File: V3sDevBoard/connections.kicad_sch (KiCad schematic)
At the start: 12 parts, among them J1 JST_ETHERNET, J2 USB_C_Receptacle_USB2.0_16P, J3 USB_C_Receptacle_USB2.0_16P, U5 CH340C

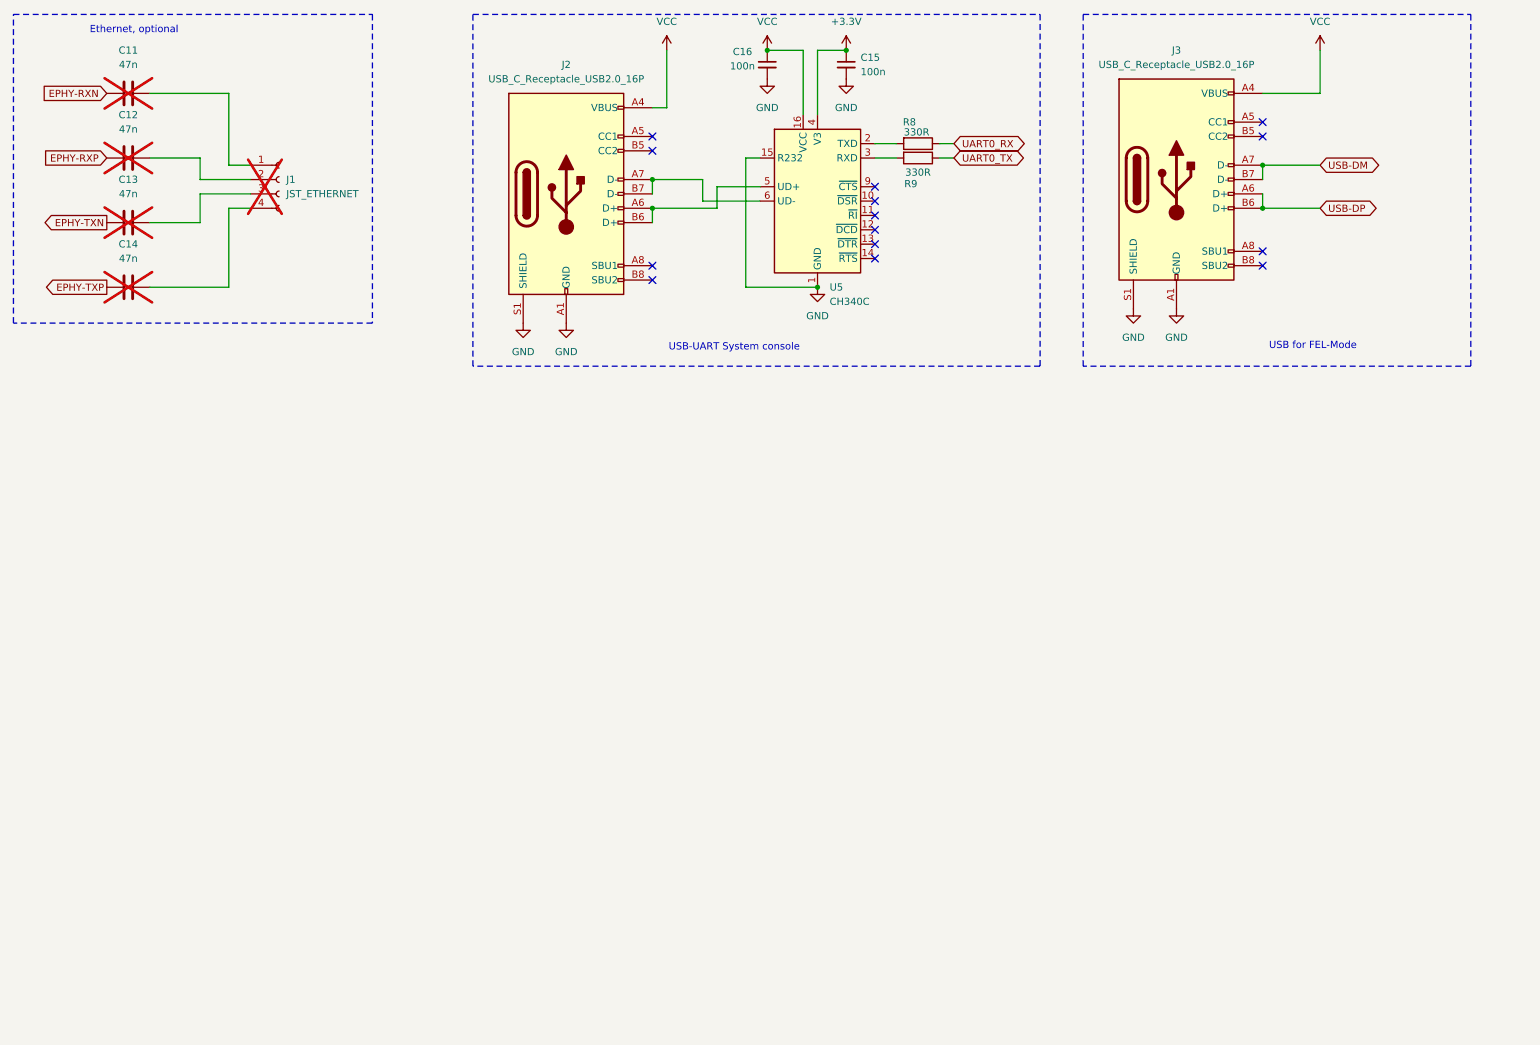
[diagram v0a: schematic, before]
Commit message: drawing schematic
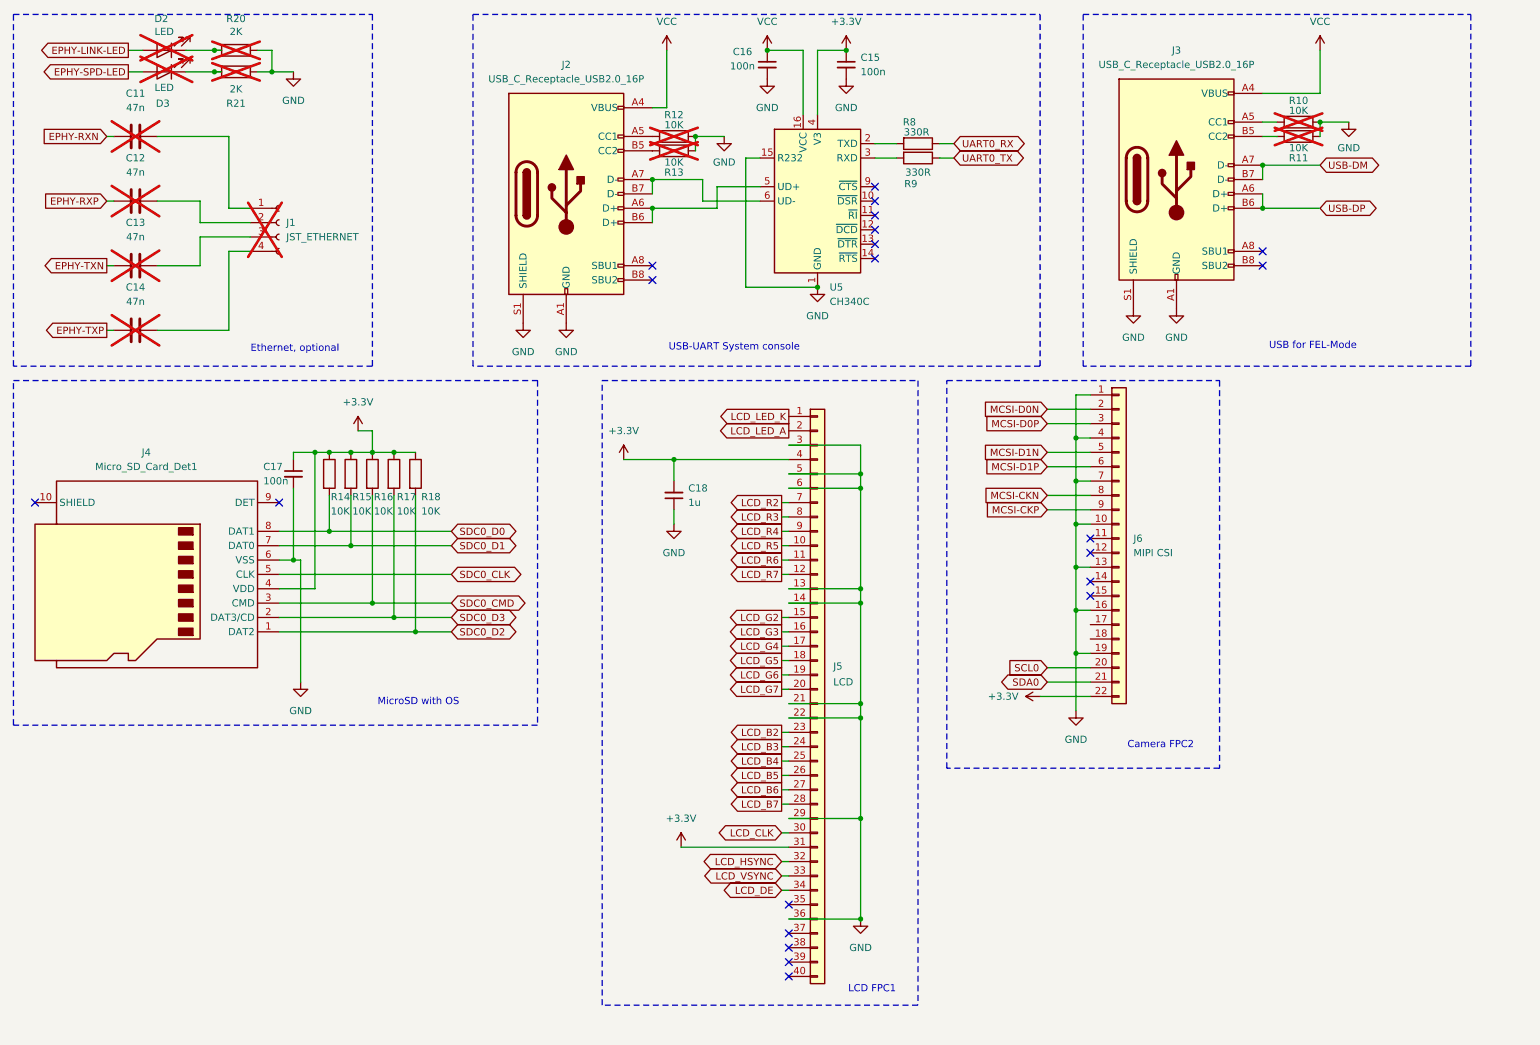
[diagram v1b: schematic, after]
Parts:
- added C17: 100n, symbol Device:C_Small
- added C18: 1u, symbol Device:C_Small
- added D2, D3: LED, LED_SMD:LED_0805_2012Metric_Pad1.15x1.40mm_HandSolder, symbol Device:LED
- added J4: Micro_SD_Card_Det1, symbol Connector:Micro_SD_Card_Det1
- added J5: LCD, Connector_FFC-FPC:Amphenol_F32Q-1A7x1-11040_1x40-1MP_P0.5mm_Horizontal, symbol Connector_Generic:Conn_01x40
- added J6: MIPI CSI, symbol Connector_Generic:Conn_01x22
- added R10, R11, R12, R13, R14, R15, R16, R17, R18: 10K, Resistor_SMD:R_0805_2012Metric_Pad1.20x1.40mm_HandSolder, symbol Device:R
- added R20, R21: 2K, Resistor_SMD:R_0805_2012Metric_Pad1.20x1.40mm_HandSolder, symbol Device:R
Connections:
- net +3.3V: now also C17.1, C18.2, J4.4 (VDD), J5.31 (Pin_31), J5.4 (Pin_4), J6.22 (Pin_22), R14.1, R15.1, R16.1, R17.1, R18.1
- net GND: now also C17.2, C18.1, J4.6 (VSS), J5.13 (Pin_13), J5.14 (Pin_14), J5.21 (Pin_21), J5.22 (Pin_22), J5.29 (Pin_29), J5.3 (Pin_3), J5.36 (Pin_36), J5.5 (Pin_5), J5.6 (Pin_6), J6.1 (Pin_1), J6.10 (Pin_10), J6.13 (Pin_13), J6.16 (Pin_16), J6.19 (Pin_19), J6.4 (Pin_4), J6.7 (Pin_7), R10.2, R11.1, R12.2, R13.1, R20.2, R21.1
- net at J2.A5 (CC1): now also R12.1
- net at J2.B5 (CC2): now also R13.2
- net at J3.A5 (CC1): now also R10.1
- net at J3.B5 (CC2): now also R11.2
- new net: D2.1 (K), R20.1
- new net: D3.1 (K), R21.2
- new net EPHY-LINK-LED: D2.2 (A)
- new net EPHY-SPD-LED: D3.2 (A)
- new net LCD_B2: J5.23 (Pin_23)
- new net LCD_B3: J5.24 (Pin_24)
- new net LCD_B4: J5.25 (Pin_25)
- new net LCD_B5: J5.26 (Pin_26)
- new net LCD_B6: J5.27 (Pin_27)
- new net LCD_B7: J5.28 (Pin_28)
- new net LCD_CLK: J5.30 (Pin_30)
- new net LCD_DE: J5.34 (Pin_34)
- new net LCD_G2: J5.15 (Pin_15)
- new net LCD_G3: J5.16 (Pin_16)
- new net LCD_G4: J5.17 (Pin_17)
- new net LCD_G5: J5.18 (Pin_18)
- new net LCD_G6: J5.19 (Pin_19)
- new net LCD_G7: J5.20 (Pin_20)
- new net LCD_HSYNC: J5.32 (Pin_32)
- new net LCD_LED_A: J5.2 (Pin_2)
- new net LCD_LED_K: J5.1 (Pin_1)
- new net LCD_R2: J5.7 (Pin_7)
- new net LCD_R3: J5.8 (Pin_8)
- new net LCD_R4: J5.9 (Pin_9)
- new net LCD_R5: J5.10 (Pin_10)
- new net LCD_R6: J5.11 (Pin_11)
- new net LCD_R7: J5.12 (Pin_12)
- new net LCD_VSYNC: J5.33 (Pin_33)
- new net MCSI-CKN: J6.8 (Pin_8)
- new net MCSI-CKP: J6.9 (Pin_9)
- new net MCSI-D0N: J6.2 (Pin_2)
- new net MCSI-D0P: J6.3 (Pin_3)
- new net MCSI-D1N: J6.5 (Pin_5)
- new net MCSI-D1P: J6.6 (Pin_6)
- new net SCL0: J6.20 (Pin_20)
- new net SDA0: J6.21 (Pin_21)
- new net SDC0_CLK: J4.5 (CLK)
- new net SDC0_CMD: J4.3 (CMD), R16.2
- new net SDC0_D0: J4.8 (DAT1), R14.2
- new net SDC0_D1: J4.7 (DAT0), R15.2
- new net SDC0_D2: J4.1 (DAT2), R18.2
- new net SDC0_D3: J4.2 (DAT3/CD), R17.2
- no-connect marks 14 -> 21
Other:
- note added: "Camera FPC2"
- note added: "LCD FPC1"
- note added: "MicroSD with OS"
- moved on the sheet: C11, C12, C13, C14, J1

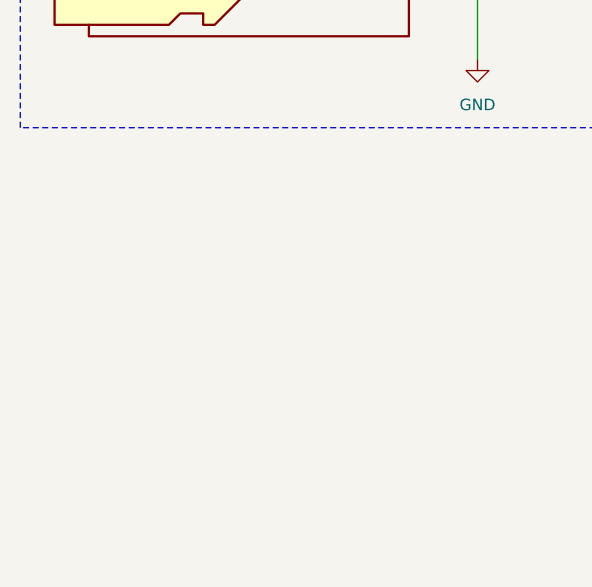
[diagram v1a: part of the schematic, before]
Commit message: drawing schematics
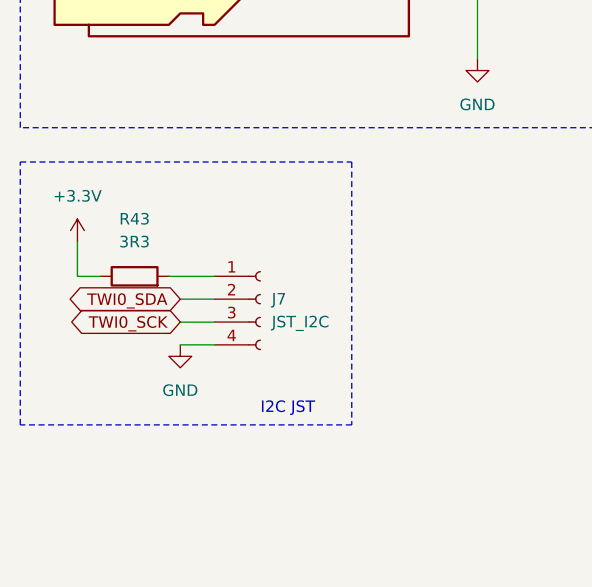
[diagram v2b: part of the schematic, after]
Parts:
- added J7: JST_I2C, Connector_JST:JST_GH_BM04B-GHS-TBT_1x04-1MP_P1.25mm_Vertical, symbol Connector:Conn_01x04_Socket
- added R43: 3R3, symbol Device:R
- J6: footprint (none) -> Connector_FFC-FPC:Amphenol_F32Q-1A7x1-11022_1x22-1MP_P0.5mm_Horizontal
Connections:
- net +3.3V: now also R43.1
- net GND: now also J7.4 (Pin_4)
- new net: J7.1 (Pin_1), R43.2
- new net TWI0_SCK: J7.3 (Pin_3)
- new net TWI0_SDA: J7.2 (Pin_2)
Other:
- note added: "I2C JST"
- company: (none) -> J.K.
- title: (none) -> V3s Dev Board

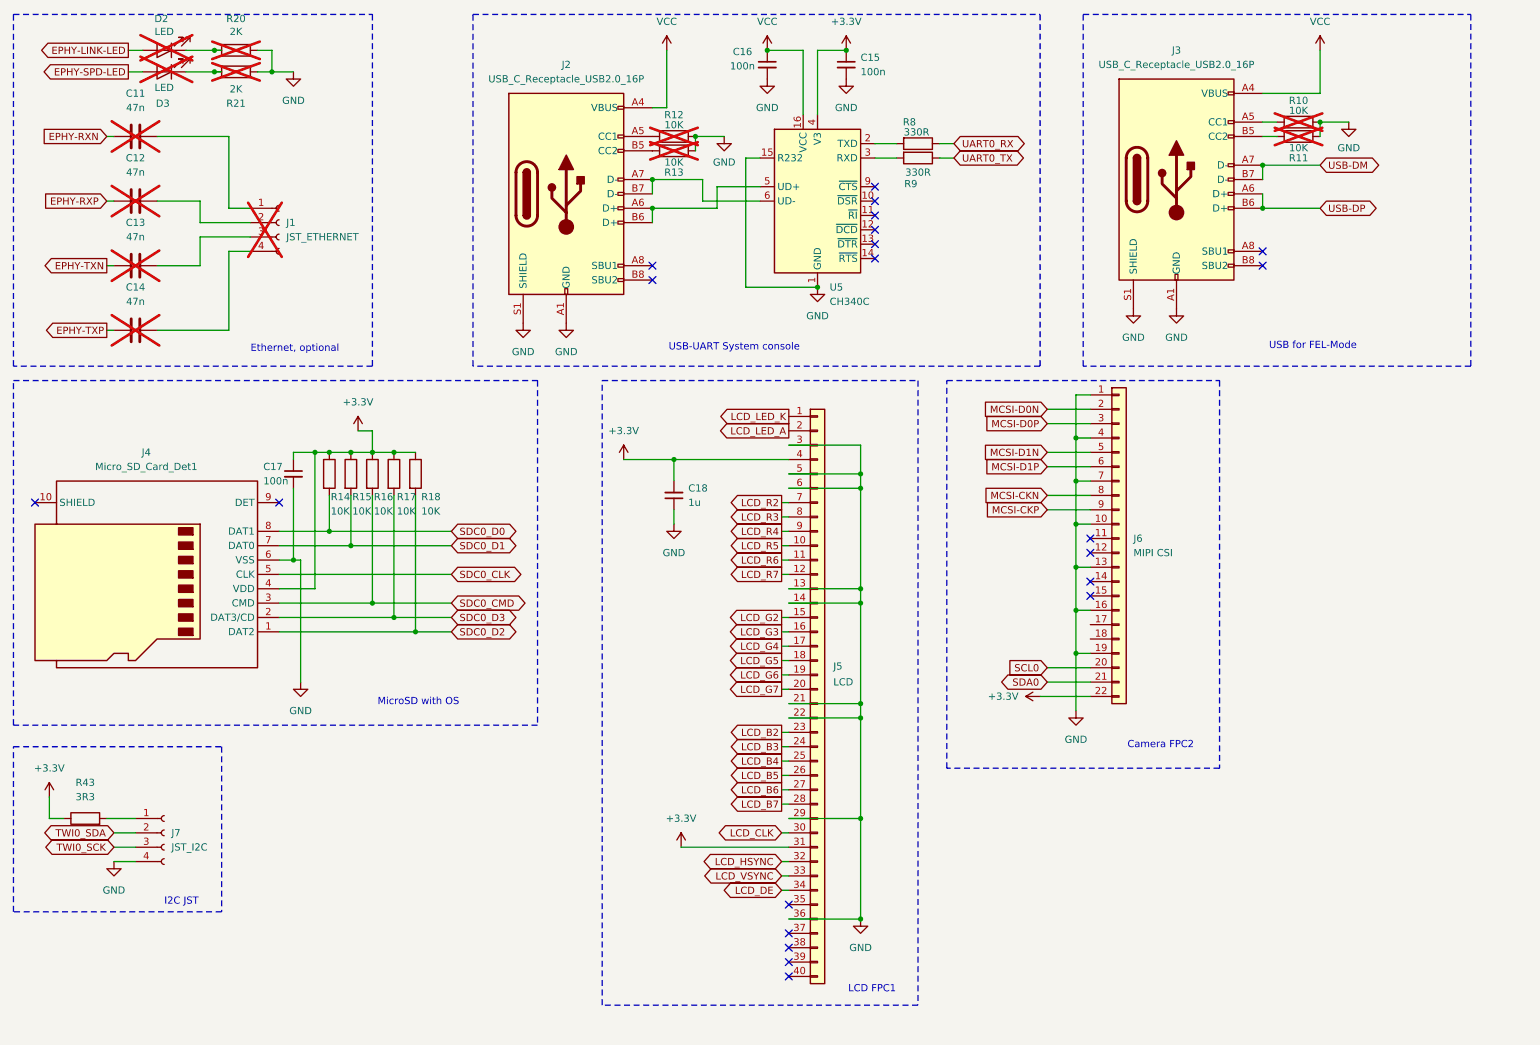
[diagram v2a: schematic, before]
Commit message: advancing in schematics and footprints
Making needed custom footprints for connectors, adding a lot of small changes to schematics.
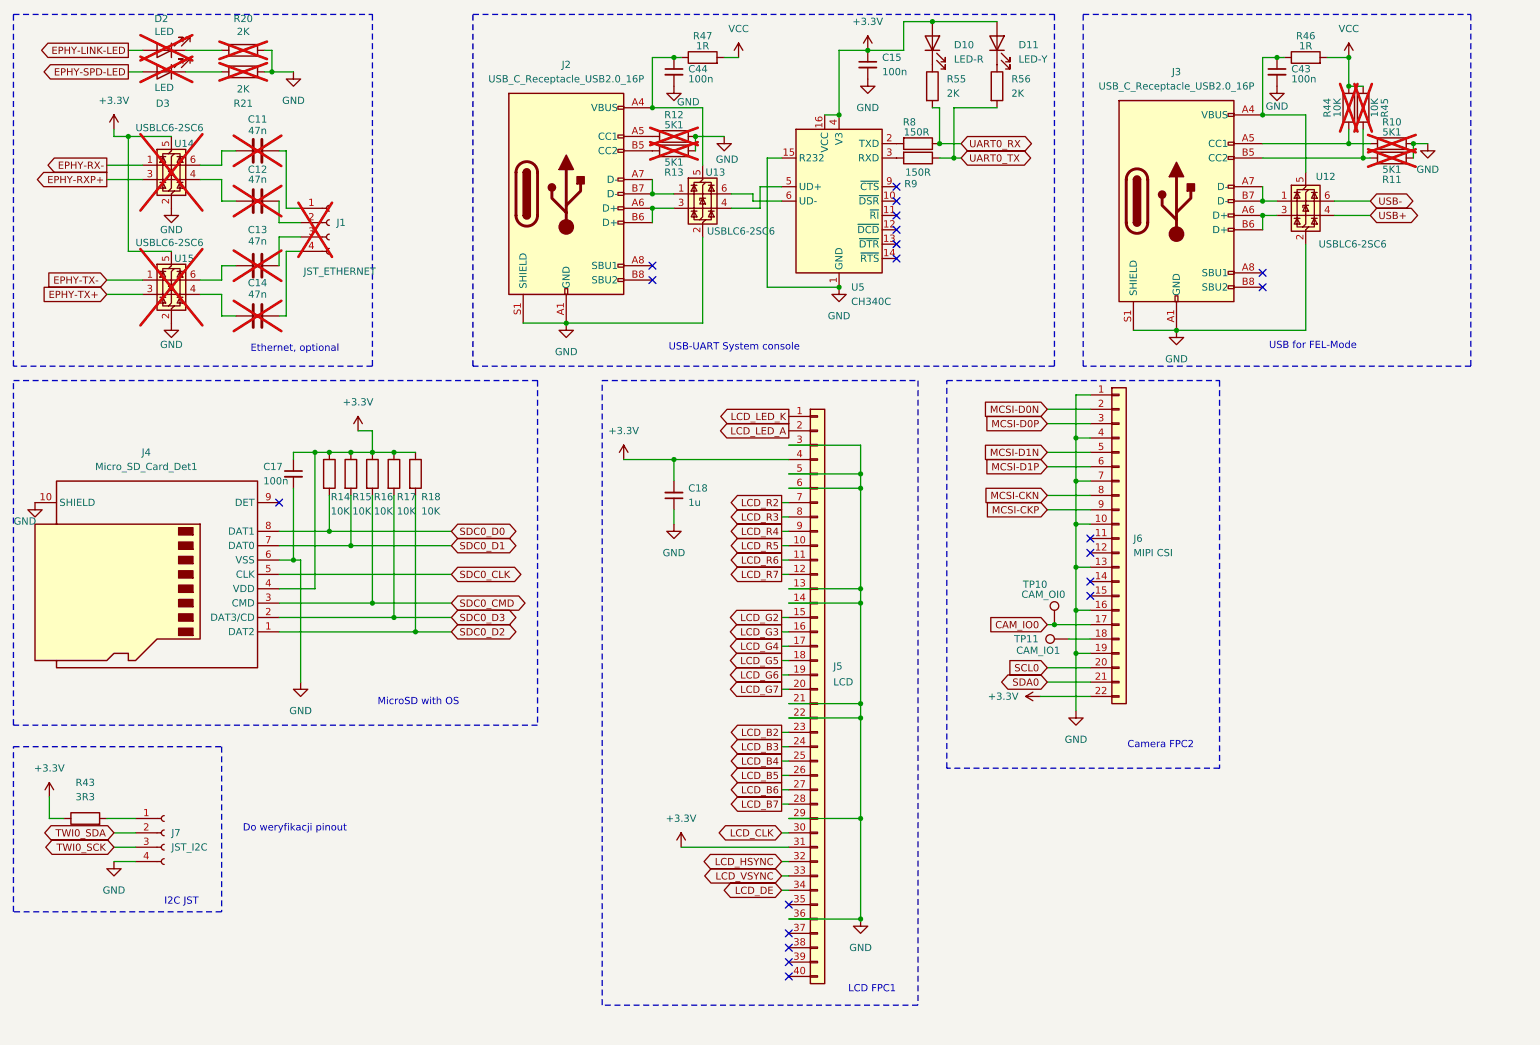
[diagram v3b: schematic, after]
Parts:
- removed C16: 100n, Capacitor_SMD:C_0805_2012Metric_Pad1.18x1.45mm_HandSolder, symbol Device:C_Small
- added C43, C44: 100n, Capacitor_SMD:C_0201_0603Metric_Pad0.64x0.40mm_HandSolder, symbol Device:C_Small
- added D10: LED-R, LED_SMD:LED_0805_2012Metric_Pad1.15x1.40mm_HandSolder, symbol Device:LED
- added D11: LED-Y, LED_SMD:LED_0805_2012Metric_Pad1.15x1.40mm_HandSolder, symbol Device:LED
- added R44, R45: 10K, Resistor_SMD:R_0805_2012Metric_Pad1.20x1.40mm_HandSolder, symbol Device:R
- added R46, R47: 1R, Resistor_SMD:R_0805_2012Metric_Pad1.20x1.40mm_HandSolder, symbol Device:R
- added R55, R56: 2K, Resistor_SMD:R_0805_2012Metric_Pad1.20x1.40mm_HandSolder, symbol Device:R
- added TP10: CAM_OI0, TestPoint:TestPoint_Pad_D1.0mm, symbol Connector:TestPoint
- added TP11: CAM_IO1, TestPoint:TestPoint_Pad_D1.0mm, symbol Connector:TestPoint
- added U12, U13, U14, U15: USBLC6-2SC6, Package_TO_SOT_SMD:SOT-23-6, symbol Power_Protection:USBLC6-2SC6
- J4: footprint (none) -> Connector_Card:microSD
- J6: footprint Connector_FFC-FPC:Amphenol_F32Q-1A7x1-11022_1x22-1MP_P0.5mm_Horizontal -> Connector_FFC-FPC:FPC_1x22-1MP_P0.5mm_Vertical
- R10, R11, R12, R13: value 10K -> 5K1
- R8, R9: value 330R -> 150R
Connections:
- net +3.3V: now also U5.16 (VCC), D10.2 (A), D11.2 (A), U14.5 (VBUS), U15.5 (VBUS)
- net GND: now also J4.10 (SHIELD), C43.2, C44.2, U12.2 (GND), U13.2 (GND), U14.2 (GND), U15.2 (GND)
- net UART0_RX: now also R55.2
- net UART0_TX: now also R56.2
- net VCC: now also R44.2, R45.1, R46.2, R47.2; no longer J2.A4 (VBUS), J2.A9 (VBUS), J2.B4 (VBUS), J2.B9 (VBUS), J3.A4 (VBUS), J3.A9 (VBUS), J3.B4 (VBUS), J3.B9 (VBUS), U5.16 (VCC)
- net at J2.A6 (D+), J2.B6 (D+): now also U13.3 (I/O2); no longer U5.5 (UD+)
- net at J2.A7 (D-), J2.B7 (D-): now also U13.1 (I/O1); no longer U5.6 (UD-)
- net CAM_IO0: now reaches J6.17 (Pin_17)
- net CAM_IO0: now also TP10.1
- net at J6.18 (Pin_18): now also TP11.1
- net at J3.A5 (CC1), R10.1: now also R44.1
- net at J3.B5 (CC2), R11.2: now also R45.2
- net EPHY-RXN: no longer names the net of C11.1
- net EPHY-RXN: now also U14.6 (I/O1)
- net EPHY-RXP: no longer names the net of C12.1
- net EPHY-RXP: now also U14.4 (I/O2)
- net EPHY-TXN: no longer names the net of C13.1
- net EPHY-TXN: now also U15.6 (I/O1)
- net EPHY-TXP: no longer names the net of C14.1
- net EPHY-TXP: now also U15.4 (I/O2)
- net USB-DM: no longer names the net of J3.A7 (D-), J3.B7 (D-)
- net USB-DM: now also U12.1 (I/O1)
- net USB-DP: no longer names the net of J3.A6 (D+), J3.B6 (D+)
- net USB-DP: now also U12.3 (I/O2)
- new net: C44.1, J2.A4 (VBUS), J2.A9 (VBUS), J2.B4 (VBUS), J2.B9 (VBUS), R47.1, U13.5 (VBUS)
- new net: D11.1 (K), R56.1
- new net: C43.1, J3.A4 (VBUS), J3.A9 (VBUS), J3.B4 (VBUS), J3.B9 (VBUS), R46.1, U12.5 (VBUS)
- new net: U13.4 (I/O2), U5.5 (UD+)
- new net: U13.6 (I/O1), U5.6 (UD-)
- new net: D10.1 (K), R55.1
- new net EPHY-RX-: U14.1 (I/O1)
- new net EPHY-RXP+: U14.3 (I/O2)
- new net EPHY-TX+: U15.3 (I/O2)
- new net EPHY-TX-: U15.1 (I/O1)
- new net USB+: U12.4 (I/O2)
- new net USB-: U12.6 (I/O1)
- no-connect marks 21 -> 20
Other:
- note added: "Do weryfikacji pinout"
- title: V3s Dev Board -> V3s_Dev_Board
- moved on the sheet: C11, C12, C13, C14, C15, J1, J3, R10, R11, R20, R21, U5
